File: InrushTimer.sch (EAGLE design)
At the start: 78 parts, among them IC1 NE555D, IC2 TLC272D, IC3 4076N, IC4 NE555D, Q2 TIP41C

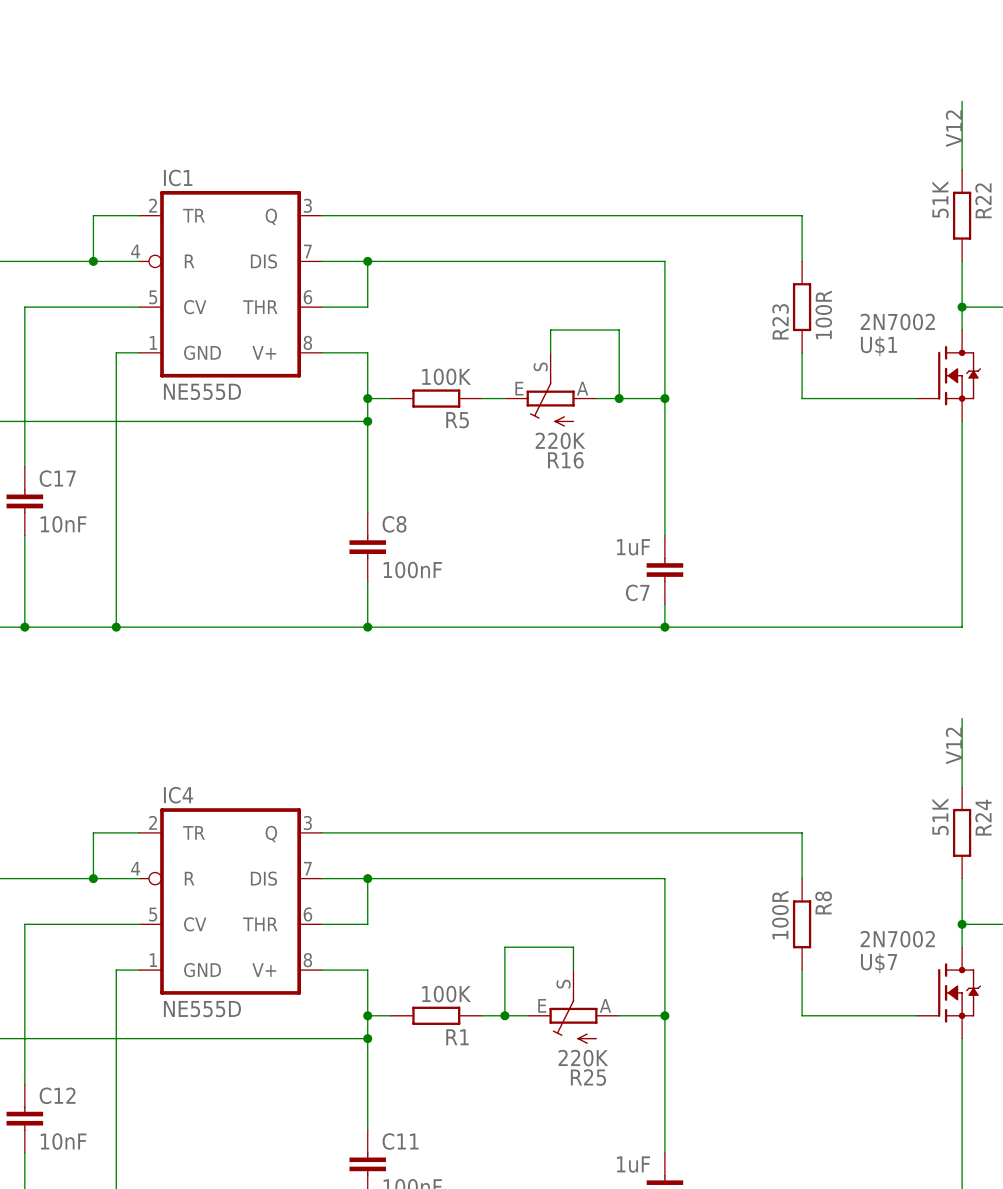
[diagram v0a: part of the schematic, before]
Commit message: Fixed an incorred footprint.
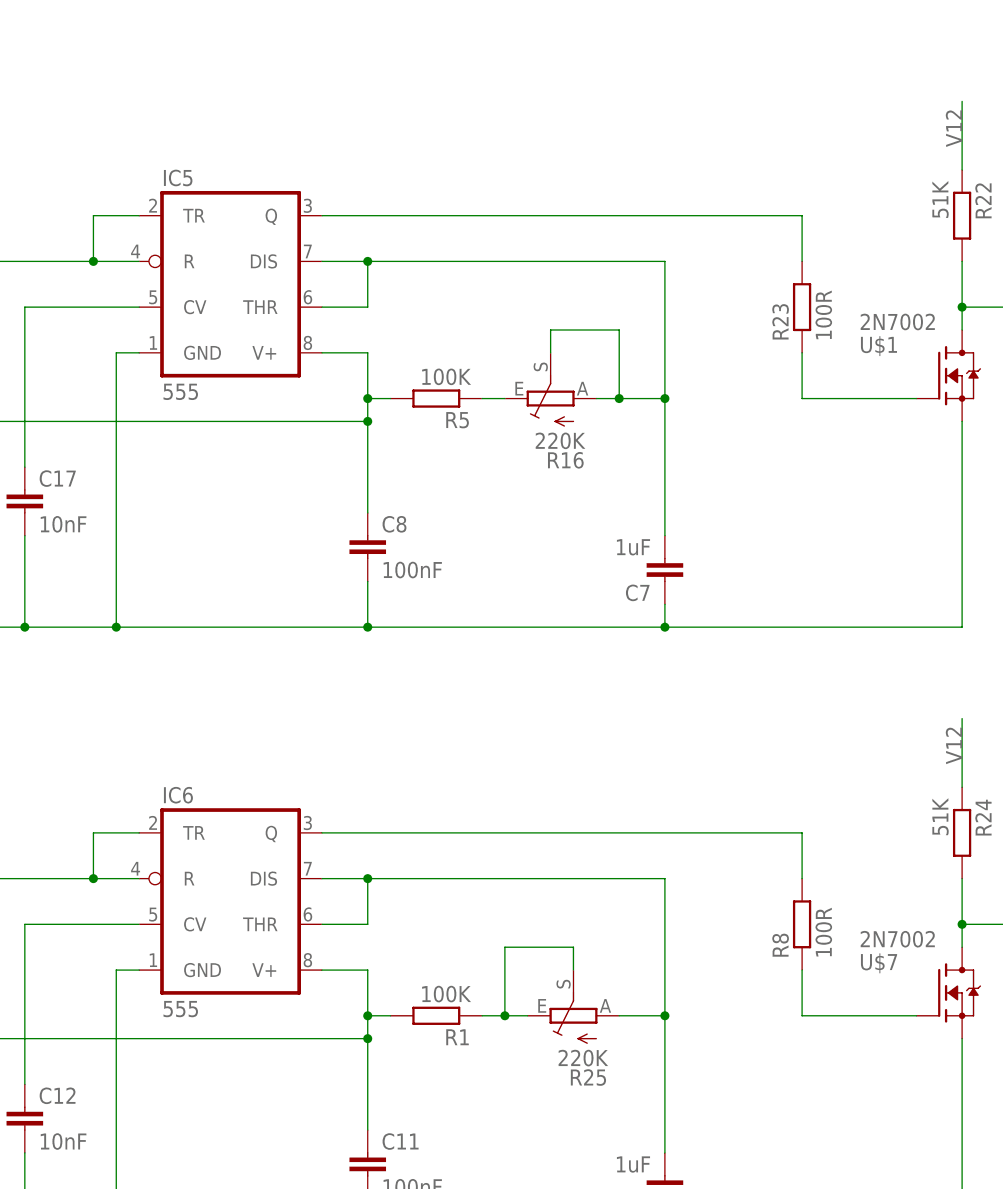
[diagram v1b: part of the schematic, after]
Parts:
- removed IC1, IC4: NE555D, linear:NE555D
- added IC5, IC6: 555, linear:555
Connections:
- net N$28: now also IC6.DIS, IC6.THR; no longer IC4.DIS, IC4.THR
- net N$35: now also IC5.CV; no longer IC1.CV
- net N$36: now also R8.1; no longer R8.2
- net N$4: now also IC5.DIS, IC5.THR; no longer IC1.DIS, IC1.THR
- net N$40: now also IC6.CV; no longer IC4.CV
- net N$47: now also IC5.Q; no longer IC1.Q
- net N$48: now also IC6.Q, R8.2; no longer IC4.Q, R8.1
- net RESET_N: now also IC5.R, IC5.TR, IC6.R, IC6.TR; no longer IC1.R, IC1.TR, IC4.R, IC4.TR
- net V12: now also IC5.V+, IC6.V+; no longer IC1.V+, IC4.V+
- net ZERO: now also IC5.GND, IC6.GND; no longer IC1.GND, IC4.GND
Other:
- moved on the sheet: R8
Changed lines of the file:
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@@
 <parts>
 <part name="D3" library="diode" deviceset="DIODE-" device="SOD323-R" value="Z12V"/>
-<part name="IC1" library="linear" deviceset="*555" device="D" technology="NE"/>
 <part name="R5" library="rcl" deviceset="R-EU_" device="0207/2V" value="100K"/>
 <part name="C2" library="rcl" deviceset="CPOL-EU" device="E2-5" value="10u"/>
@@
 <part name="C10" library="rcl" deviceset="C-EU" device="C0805K" value="1nF"/>
 <part name="C1" library="rcl" deviceset="C-EU" device="C1206K" value="100nF"/>
-<part name="IC4" library="linear" deviceset="*555" device="D" technology="NE"/>
 <part name="R1" library="rcl" deviceset="R-EU_" device="0207/2V" value="100K"/>
 <part name="C6" library="rcl" deviceset="C-EU" device="C1206K" value="1uF"/>
@@
 <part name="SJ2" library="jumper" deviceset="SJ" device=""/>
 <part name="C3" library="rcl" deviceset="C-EU" device="050-024X044" value="100nF"/>
+<part name="IC5" library="linear" deviceset="*555" device=""/>
+<part name="IC6" library="linear" deviceset="*555" device=""/>
 </parts>
 <sheets>
@@
 <instances>
 <instance part="D3" gate="G$1" x="66.04" y="38.1" rot="R90"/>
-<instance part="IC1" gate="A" x="210.82" y="45.72"/>
 <instance part="R5" gate="G$1" x="233.68" y="33.02" rot="R180"/>
 <instance part="C2" gate="G$1" x="55.88" y="50.8"/>
@@
 <instance part="C10" gate="G$1" x="119.38" y="129.54" rot="R90"/>
 <instance part="C1" gate="G$1" x="127" y="162.56"/>
-<instance part="IC4" gate="A" x="210.82" y="-22.86"/>
 <instance part="R1" gate="G$1" x="233.68" y="-35.56" rot="R180"/>
 <instance part="C6" gate="G$1" x="259.08" y="-55.88" rot="R180"/>
@@
 <attribute name="NAME" x="280.67" y="-30.48" size="1.778" layer="95"/>
 </instance>
-<instance part="R8" gate="G$1" x="274.32" y="-25.4" rot="R270"/>
+<instance part="R8" gate="G$1" x="274.32" y="-25.4" rot="R90"/>
 <instance part="R24" gate="G$1" x="292.1" y="-15.24" rot="R270"/>
 <instance part="C11" gate="G$1" x="226.06" y="-50.8"/>
@@
 <instance part="SJ2" gate="1" x="490.22" y="-15.24" rot="R90"/>
 <instance part="C3" gate="G$1" x="327.66" y="-10.16"/>
+<instance part="IC5" gate="A" x="210.82" y="45.72"/>
+<instance part="IC6" gate="A" x="210.82" y="-22.86"/>
 </instances>
 <busses>
@@
 <segment>
 <wire x1="226.06" y1="20.32" x2="226.06" y2="30.48" width="0.1524" layer="91"/>
-<pinref part="IC1" gate="A" pin="V+"/>
 <wire x1="220.98" y1="38.1" x2="226.06" y2="38.1" width="0.1524" layer="91"/>
 <wire x1="226.06" y1="30.48" x2="226.06" y2="33.02" width="0.1524" layer="91"/>
@@
 <wire x1="228.6" y1="33.02" x2="226.06" y2="33.02" width="0.1524" layer="91"/>
 <junction x="226.06" y="33.02"/>
+<pinref part="IC5" gate="A" pin="V+"/>
 </segment>
 <segment>
@@
 <segment>
 <wire x1="226.06" y1="-48.26" x2="226.06" y2="-38.1" width="0.1524" layer="91"/>
-<pinref part="IC4" gate="A" pin="V+"/>
 <wire x1="220.98" y1="-30.48" x2="226.06" y2="-30.48" width="0.1524" layer="91"/>
 <wire x1="226.06" y1="-38.1" x2="226.06" y2="-35.56" width="0.1524" layer="91"/>
@@
 <wire x1="228.6" y1="-35.56" x2="226.06" y2="-35.56" width="0.1524" layer="91"/>
 <junction x="226.06" y="-35.56"/>
+<pinref part="IC6" gate="A" pin="V+"/>
 </segment>
 <segment>
@@
 <wire x1="259.08" y1="7.62" x2="226.06" y2="7.62" width="0.1524" layer="91"/>
 <wire x1="226.06" y1="7.62" x2="198.12" y2="7.62" width="0.1524" layer="91"/>
-<pinref part="IC1" gate="A" pin="GND"/>
 <wire x1="200.66" y1="38.1" x2="198.12" y2="38.1" width="0.1524" layer="91"/>
 <wire x1="198.12" y1="38.1" x2="198.12" y2="7.62" width="0.1524" layer="91"/>
@@
 <wire x1="292.1" y1="7.62" x2="259.08" y2="7.62" width="0.1524" layer="91"/>
 <junction x="259.08" y="7.62"/>
+<pinref part="IC5" gate="A" pin="GND"/>
 </segment>
 <segment>
@@
 <wire x1="259.08" y1="-60.96" x2="226.06" y2="-60.96" width="0.1524" layer="91"/>
 <wire x1="226.06" y1="-60.96" x2="198.12" y2="-60.96" width="0.1524" layer="91"/>
-<pinref part="IC4" gate="A" pin="GND"/>
 <wire x1="200.66" y1="-30.48" x2="198.12" y2="-30.48" width="0.1524" layer="91"/>
 <wire x1="198.12" y1="-30.48" x2="198.12" y2="-60.96" width="0.1524" layer="91"/>
@@
 <wire x1="292.1" y1="-60.96" x2="259.08" y2="-60.96" width="0.1524" layer="91"/>
 <junction x="259.08" y="-60.96"/>
+<pinref part="IC6" gate="A" pin="GND"/>
 </segment>
 <segment>
@@
 </segment>
 <segment>
-<pinref part="IC1" gate="A" pin="R"/>
 <wire x1="200.66" y1="48.26" x2="195.58" y2="48.26" width="0.1524" layer="91"/>
-<pinref part="IC1" gate="A" pin="TR"/>
 <wire x1="200.66" y1="53.34" x2="195.58" y2="53.34" width="0.1524" layer="91"/>
 <wire x1="195.58" y1="53.34" x2="195.58" y2="48.26" width="0.1524" layer="91"/>
-<wire x1="195.58" y1="48.26" x2="165.1" y2="48.26" width="0.1524" layer="91"/>
 <junction x="195.58" y="48.26"/>
 <label x="165.1" y="48.26" size="1.778" layer="95"/>
-</segment>
-<segment>
-<pinref part="IC4" gate="A" pin="R"/>
+<wire x1="195.58" y1="48.26" x2="165.1" y2="48.26" width="0.1524" layer="91"/>
+<pinref part="IC5" gate="A" pin="TR"/>
+<pinref part="IC5" gate="A" pin="R"/>
+</segment>
+<segment>
 <wire x1="200.66" y1="-20.32" x2="195.58" y2="-20.32" width="0.1524" layer="91"/>
-<pinref part="IC4" gate="A" pin="TR"/>
 <wire x1="200.66" y1="-15.24" x2="195.58" y2="-15.24" width="0.1524" layer="91"/>
 <wire x1="195.58" y1="-15.24" x2="195.58" y2="-20.32" width="0.1524" layer="91"/>
@@
 <junction x="195.58" y="-20.32"/>
 <label x="165.1" y="-20.32" size="1.778" layer="95"/>
+<pinref part="IC6" gate="A" pin="TR"/>
+<pinref part="IC6" gate="A" pin="R"/>
 </segment>
 </net>
@@
 <net name="N$35" class="0">
 <segment>
-<pinref part="IC1" gate="A" pin="CV"/>
 <wire x1="200.66" y1="43.18" x2="187.96" y2="43.18" width="0.1524" layer="91"/>
 <wire x1="187.96" y1="25.4" x2="187.96" y2="43.18" width="0.1524" layer="91"/>
 <pinref part="C17" gate="G$1" pin="1"/>
+<pinref part="IC5" gate="A" pin="CV"/>
 </segment>
 </net>
@@
 <net name="N$28" class="0">
 <segment>
-<pinref part="IC4" gate="A" pin="DIS"/>
-<pinref part="IC4" gate="A" pin="THR"/>
 <wire x1="226.06" y1="-20.32" x2="220.98" y2="-20.32" width="0.1524" layer="91"/>
 <wire x1="220.98" y1="-25.4" x2="226.06" y2="-25.4" width="0.1524" layer="91"/>
@@
 <pinref part="R25" gate="1" pin="A"/>
 <wire x1="259.08" y1="-35.56" x2="254" y2="-35.56" width="0.1524" layer="91"/>
+<pinref part="IC6" gate="A" pin="THR"/>
+<pinref part="IC6" gate="A" pin="DIS"/>
 </segment>
 </net>
@@
 <pinref part="U$7" gate="G$1" pin="G"/>
 <wire x1="287.02" y1="-35.56" x2="274.32" y2="-35.56" width="0.1524" layer="91"/>
-<pinref part="R8" gate="G$1" pin="2"/>
-<wire x1="274.32" y1="-35.56" x2="274.32" y2="-30.48" width="0.1524" layer="91"/>
+<pinref part="R8" gate="G$1" pin="1"/>
+<wire x1="274.32" y1="-30.48" x2="274.32" y2="-35.56" width="0.1524" layer="91"/>
 </segment>
 </net>
 <net name="N$40" class="0">
 <segment>
-<pinref part="IC4" gate="A" pin="CV"/>
 <wire x1="200.66" y1="-25.4" x2="187.96" y2="-25.4" width="0.1524" layer="91"/>
 <wire x1="187.96" y1="-43.18" x2="187.96" y2="-25.4" width="0.1524" layer="91"/>
 <pinref part="C12" gate="G$1" pin="1"/>
+<pinref part="IC6" gate="A" pin="CV"/>
 </segment>
 </net>
 <net name="N$47" class="0">
 <segment>
-<pinref part="IC1" gate="A" pin="Q"/>
 <pinref part="R23" gate="G$1" pin="2"/>
 <wire x1="220.98" y1="53.34" x2="274.32" y2="53.34" width="0.1524" layer="91"/>
 <wire x1="274.32" y1="53.34" x2="274.32" y2="48.26" width="0.1524" layer="91"/>
+<pinref part="IC5" gate="A" pin="Q"/>
 </segment>
 </net>
 <net name="N$48" class="0">
 <segment>
-<pinref part="IC4" gate="A" pin="Q"/>
 <wire x1="274.32" y1="-15.24" x2="220.98" y2="-15.24" width="0.1524" layer="91"/>
-<pinref part="R8" gate="G$1" pin="1"/>
+<pinref part="IC6" gate="A" pin="Q"/>
+<pinref part="R8" gate="G$1" pin="2"/>
 <wire x1="274.32" y1="-20.32" x2="274.32" y2="-15.24" width="0.1524" layer="91"/>
 </segment>
@@
 <pinref part="R16" gate="1" pin="A"/>
 <wire x1="254" y1="33.02" x2="251.46" y2="33.02" width="0.1524" layer="91"/>
-<pinref part="IC1" gate="A" pin="DIS"/>
-<pinref part="IC1" gate="A" pin="THR"/>
 <wire x1="226.06" y1="48.26" x2="220.98" y2="48.26" width="0.1524" layer="91"/>
 <wire x1="220.98" y1="43.18" x2="226.06" y2="43.18" width="0.1524" layer="91"/>
@@
 <junction x="254" y="33.02"/>
 <junction x="259.08" y="33.02"/>
-</segment>
-</net>
+<pinref part="IC5" gate="A" pin="THR"/>
+<pinref part="IC5" gate="A" pin="DIS"/>
+</segment>
+</net>

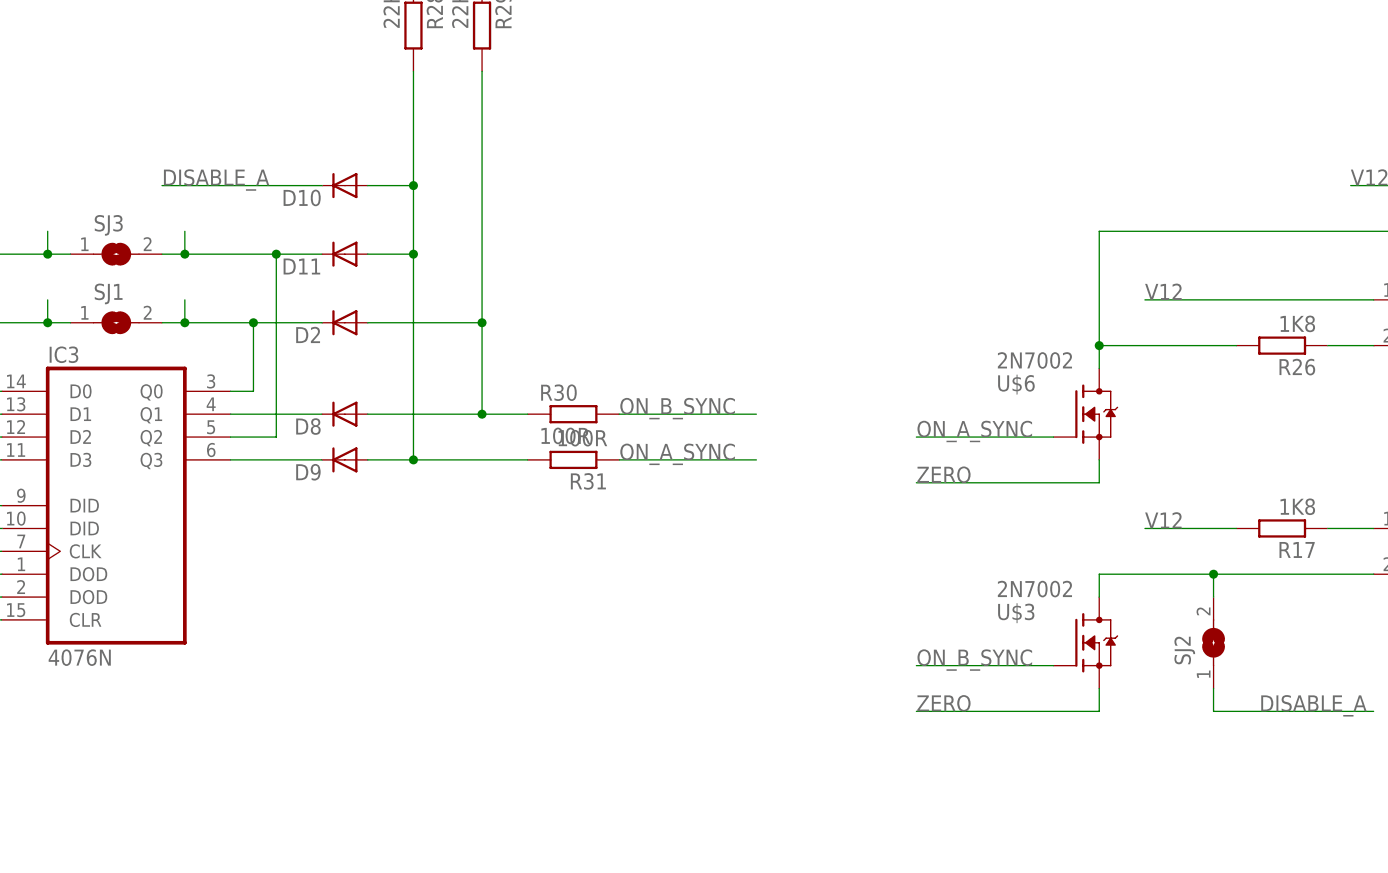
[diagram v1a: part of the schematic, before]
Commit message: Tidied up some traces and improved trace seraration.
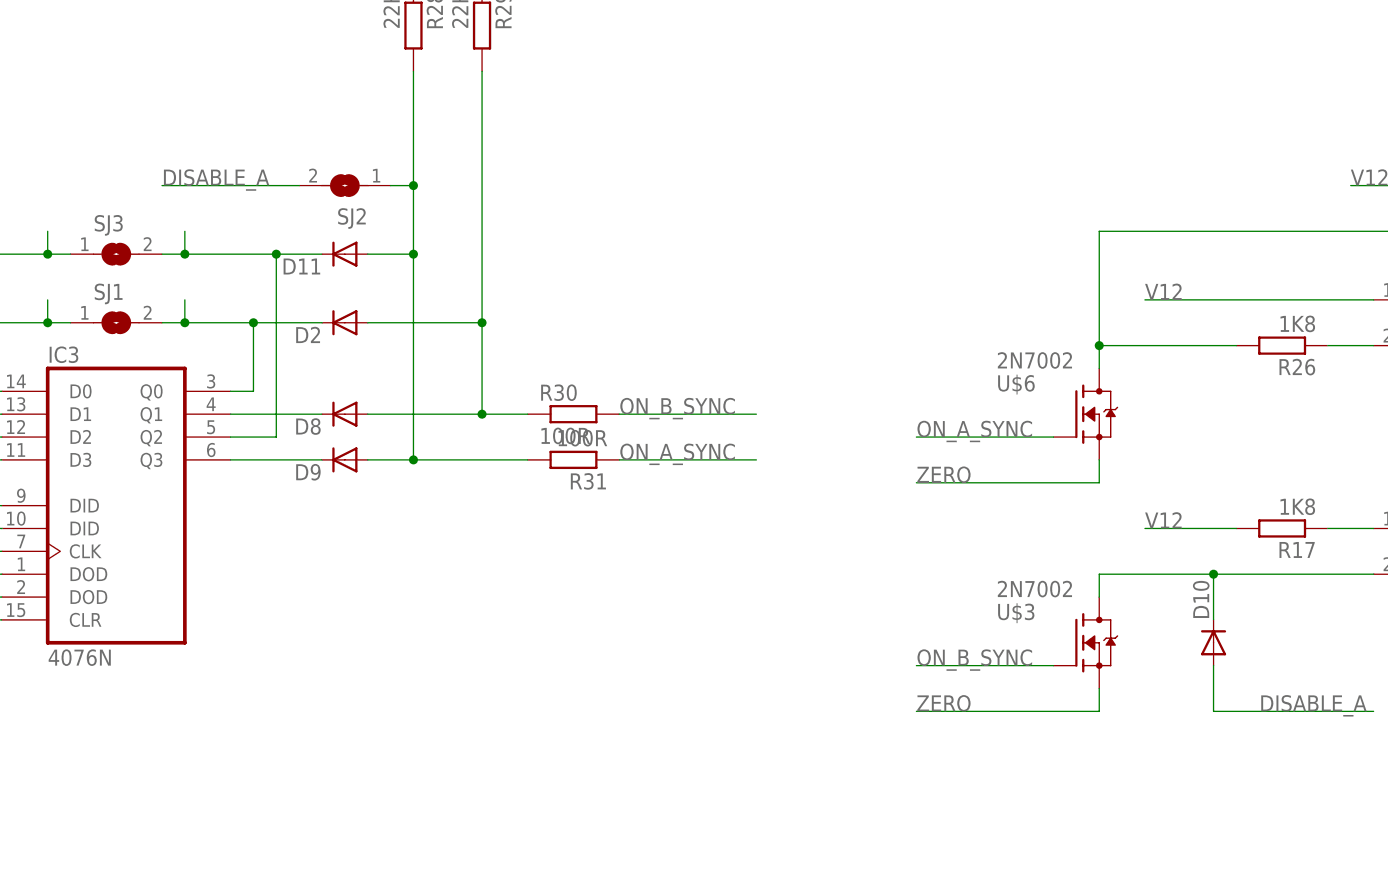
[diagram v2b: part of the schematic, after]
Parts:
- D7: device diode:DIODE-DO41-7.6 -> diode:DIODE-DO41-10
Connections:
- net DISABLE_A: now also D10.A, SJ2.2; no longer D10.C, SJ2.1
- net N$33: now also D10.C; no longer SJ2.2
- net N$34: now also SJ2.1; no longer D10.A
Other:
- moved on the sheet: D10, SJ2
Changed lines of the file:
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@@
 <part name="D12" library="diode" deviceset="BZX55" device=""/>
 <part name="D1" library="diode" deviceset="BZX55" device=""/>
-<part name="D7" library="diode" deviceset="DIODE-" device="DO41-7.6"/>
+<part name="D7" library="diode" deviceset="DIODE-" device="DO41-10"/>
 <part name="IC2" library="linear" deviceset="TLC272" device="D" value="TLC272D"/>
 <part name="C4" library="rcl" deviceset="C-EU" device="050-024X044" value="100nF"/>
@@
 <attribute name="NAME" x="391.16" y="4.5974" size="1.778" layer="95" rot="R180"/>
 </instance>
-<instance part="D10" gate="G$1" x="393.7" y="35.56" smashed="yes" rot="R180">
-<attribute name="NAME" x="391.16" y="35.0774" size="1.778" layer="95" rot="R180"/>
+<instance part="D10" gate="G$1" x="490.22" y="-15.24" smashed="yes" rot="R90">
+<attribute name="NAME" x="489.7374" y="-12.7" size="1.778" layer="95" rot="R90"/>
 </instance>
 <instance part="D11" gate="G$1" x="393.7" y="27.94" smashed="yes" rot="R180">
@@
 <attribute name="NAME" x="391.16" y="19.8374" size="1.778" layer="95" rot="R180"/>
 </instance>
-<instance part="SJ2" gate="1" x="490.22" y="-15.24" rot="R90"/>
+<instance part="SJ2" gate="1" x="393.7" y="35.56" rot="R180"/>
 <instance part="C3" gate="G$1" x="327.66" y="-10.16"/>
 <instance part="IC5" gate="A" x="210.82" y="45.72"/>
@@
 <pinref part="U$8" gate="G$1" pin="C"/>
 <wire x1="508" y1="-7.62" x2="490.22" y2="-7.62" width="0.1524" layer="91"/>
-<pinref part="SJ2" gate="1" pin="2"/>
+<pinref part="D10" gate="G$1" pin="C"/>
 <wire x1="490.22" y1="-7.62" x2="477.52" y2="-7.62" width="0.1524" layer="91"/>
-<wire x1="490.22" y1="-10.16" x2="490.22" y2="-7.62" width="0.1524" layer="91"/>
+<wire x1="490.22" y1="-12.7" x2="490.22" y2="-7.62" width="0.1524" layer="91"/>
 <junction x="490.22" y="-7.62"/>
 </segment>
@@
 <wire x1="401.32" y1="5.08" x2="401.32" y2="27.94" width="0.1524" layer="91"/>
 <wire x1="401.32" y1="27.94" x2="401.32" y2="35.56" width="0.1524" layer="91"/>
+<pinref part="D11" gate="G$1" pin="A"/>
 <wire x1="401.32" y1="35.56" x2="401.32" y2="48.26" width="0.1524" layer="91"/>
-<pinref part="D10" gate="G$1" pin="A"/>
-<wire x1="396.24" y1="35.56" x2="401.32" y2="35.56" width="0.1524" layer="91"/>
-<junction x="401.32" y="35.56"/>
-<pinref part="D11" gate="G$1" pin="A"/>
 <wire x1="396.24" y1="27.94" x2="401.32" y2="27.94" width="0.1524" layer="91"/>
 <junction x="401.32" y="27.94"/>
@@
 <wire x1="414.02" y1="5.08" x2="401.32" y2="5.08" width="0.1524" layer="91"/>
 <junction x="401.32" y="5.08"/>
+<pinref part="SJ2" gate="1" pin="1"/>
+<wire x1="398.78" y1="35.56" x2="401.32" y2="35.56" width="0.1524" layer="91"/>
+<junction x="401.32" y="35.56"/>
 </segment>
 </net>
@@
 <wire x1="490.22" y1="-22.86" x2="508" y2="-22.86" width="0.1524" layer="91"/>
 <label x="495.3" y="-22.86" size="1.778" layer="95"/>
-<pinref part="SJ2" gate="1" pin="1"/>
-<wire x1="490.22" y1="-20.32" x2="490.22" y2="-22.86" width="0.1524" layer="91"/>
-</segment>
-<segment>
-<pinref part="D10" gate="G$1" pin="C"/>
-<wire x1="391.16" y1="35.56" x2="373.38" y2="35.56" width="0.1524" layer="91"/>
+<pinref part="D10" gate="G$1" pin="A"/>
+<wire x1="490.22" y1="-22.86" x2="490.22" y2="-17.78" width="0.1524" layer="91"/>
+</segment>
+<segment>
+<pinref part="SJ2" gate="1" pin="2"/>
+<wire x1="388.62" y1="35.56" x2="373.38" y2="35.56" width="0.1524" layer="91"/>
 <label x="373.38" y="35.56" size="1.778" layer="95"/>
 </segment>
